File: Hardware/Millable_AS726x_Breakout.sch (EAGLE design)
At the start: 24 parts, among them J2 Serial Interface, U1 AS726X, U3 4MB Flash

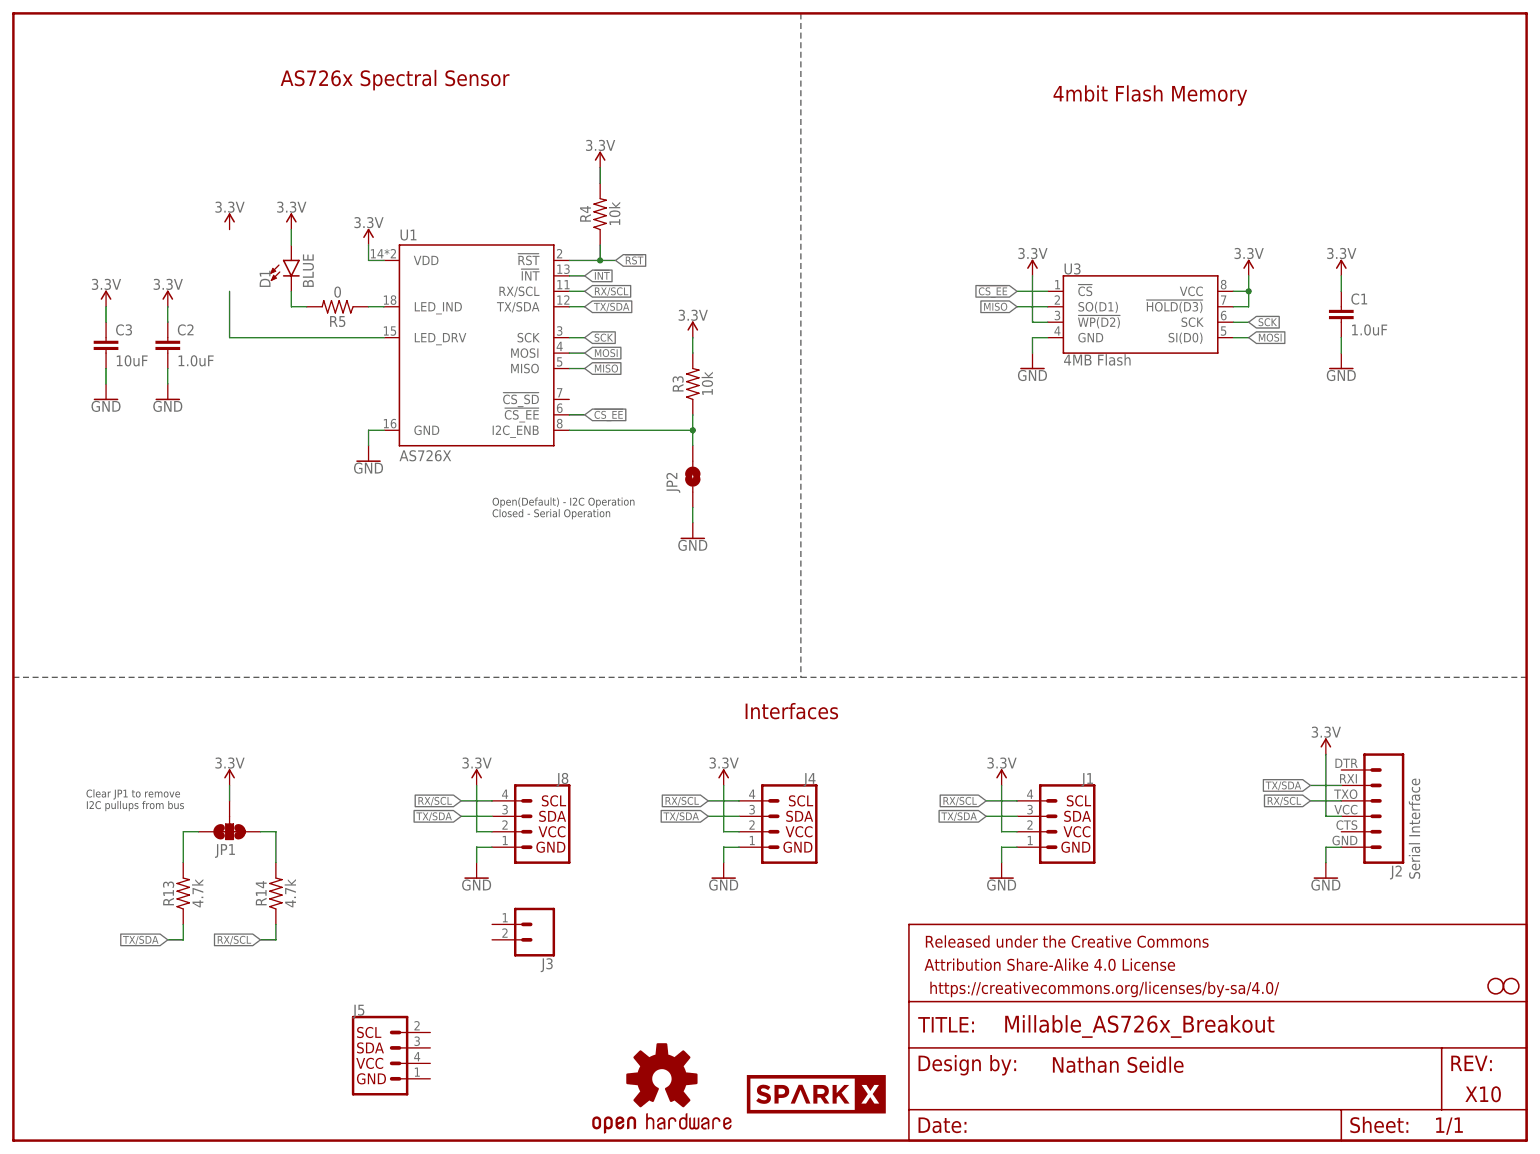
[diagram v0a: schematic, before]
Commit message: Adding firmware, panel, and small fix to dimension on main layout.
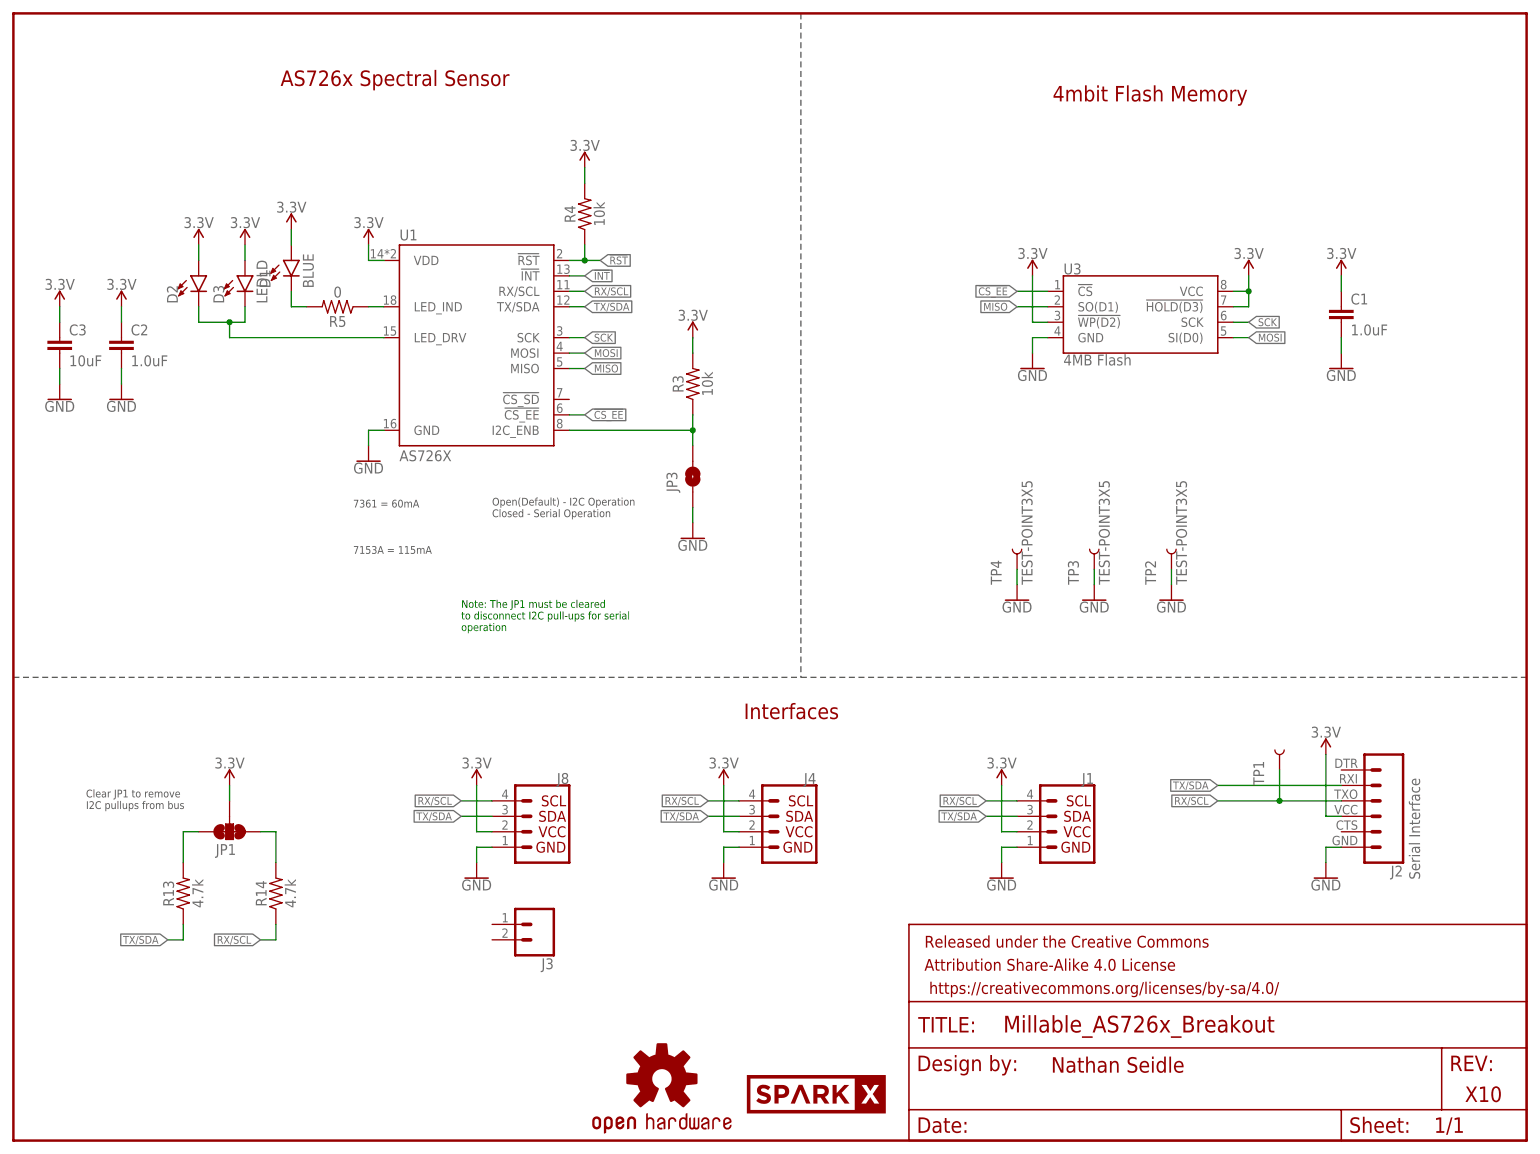
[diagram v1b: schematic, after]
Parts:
- removed H2, H4: STAND-OFF, SparkFun-Hardware:STAND-OFF
- removed J5: (no value), SparkX:I2C_STANDARDSR
- removed JP2: JUMPER-SMT_2_NO_SILK, SparkFun-Jumpers:JUMPER-SMT_2_NO_SILK
- added D2: (no value), SparkFun-LED:LED5MM
- added D3: LEDLD, SparkX:LEDLD
- added JP3: JUMPER-SMT_2_NO-MILLABLE_NO-SILK, SparkX:JUMPER-SMT_2_NO-MILLABLE_NO-SILK
- added TP1, TP2, TP3, TP4: TEST-POINT3X5, SparkFun-Connectors:TEST-POINT3X5
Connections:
- removed net N$1: JP2.2, R3.1, U1.I2C_ENB
- new net I2C_ENB: JP3.2, R3.1, U1.I2C_ENB
- net 3.3V: now also D2.A, D3.A
- net GND: now also JP3.1, TP2.1, TP3.1, TP4.1; no longer JP2.1
- net N$6: now also D2.C, D3.C
- net RX/SCL: now also TP1.1
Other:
- note added: "7153A = 115mA"
- note added: "7361 = 60mA"
- note added: "Note: The JP1 must be cleared to disconnect I2C pull-ups for serial operation"
- moved on the sheet: C2, C3, R4
